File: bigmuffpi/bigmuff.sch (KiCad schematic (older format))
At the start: 63 parts, among them J1 PWR JACK, J4 OUTPUT, J5 INPUT, Q1 BC239, Q2 BC239, Q3 BC239, Q4 BC239

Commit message: add: assign footprint to PPTC
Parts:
- F1: footprint 1206 -> Capacitor_THT:C_Disc_D8.0mm_W2.5mm_P5.00mm
- gave numbers to parts that had none: 3
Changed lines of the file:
@@
 F 0 "F1" H 2650 5650 45  0000 C CNN
 F 1 "PPTC_HALF-AMP" H 2650 5550 45  0000 C CNN
-F 2 "1206" H 2600 5950 20  0001 C CNN
+F 2 "Capacitor_THT:C_Disc_D8.0mm_W2.5mm_P5.00mm" H 2600 5950 20  0001 C CNN
 F 3 "" H 2600 5750 50  0001 C CNN
 F 4 "RES-08585" H 2650 5450 60  0000 C CNN "Field4"
@@
 	1450 5350 3450 5350
 $Comp
-L Connector:TestPoint TP?
+L Connector:TestPoint TP7
 U 1 1 5F5852AE
 P 2450 3250
-F 0 "TP?" H 2300 3250 50  0000 R CNN
+F 0 "TP7" H 2300 3250 50  0000 R CNN
 F 1 "TestPoint" H 2400 3350 50  0000 R CNN
 F 2 "TestPoint:TestPoint_Pad_2.0x2.0mm" H 2650 3250 50  0001 C CNN
@@
 Connection ~ 2450 3300
 $Comp
-L Connector:TestPoint TP?
+L Connector:TestPoint TP8
 U 1 1 5F59ACBE
 P 4500 2500
-F 0 "TP?" H 4350 2500 50  0000 R CNN
+F 0 "TP8" H 4350 2500 50  0000 R CNN
 F 1 "TestPoint" H 4450 2600 50  0000 R CNN
 F 2 "TestPoint:TestPoint_Pad_2.0x2.0mm" H 4700 2500 50  0001 C CNN
@@
 Connection ~ 4500 2550
 $Comp
-L Connector:TestPoint TP?
+L Connector:TestPoint TP9
 U 1 1 5F5A9929
 P 6350 2500
-F 0 "TP?" H 6200 2500 50  0000 R CNN
+F 0 "TP9" H 6200 2500 50  0000 R CNN
 F 1 "TestPoint" H 6300 2600 50  0000 R CNN
 F 2 "TestPoint:TestPoint_Pad_2.0x2.0mm" H 6550 2500 50  0001 C CNN

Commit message: fix: minor name fix for PPTC
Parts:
- F1: value PPTC_HALF-AMP -> PPTC
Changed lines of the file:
@@
 P 2600 5750
 F 0 "F1" H 2650 5650 45  0000 C CNN
-F 1 "PPTC_HALF-AMP" H 2650 5550 45  0000 C CNN
+F 1 "PPTC" H 2650 5550 45  0000 C CNN
 F 2 "Capacitor_THT:C_Disc_D8.0mm_W2.5mm_P5.00mm" H 2600 5950 20  0001 C CNN
 F 3 "" H 2600 5750 50  0001 C CNN
-F 4 "RES-08585" H 2650 5450 60  0000 C CNN "Field4"
+F 4 "RES-08585" H 2650 5450 60  0001 C CNN "Field4"
 	1    2600 5750
 	1    0    0    -1

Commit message: add: pick PPTC component on mouser
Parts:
- F1: Mfr. No (none) -> MF-R020; Mouser (none) -> 652-MF-R020; Supplier (none) -> Mouser
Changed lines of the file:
@@
 F 1 "PPTC" H 2650 5550 45  0000 C CNN
 F 2 "Capacitor_THT:C_Disc_D8.0mm_W2.5mm_P5.00mm" H 2600 5950 20  0001 C CNN
-F 3 "" H 2600 5750 50  0001 C CNN
+F 3 "https://cz.mouser.com/datasheet/2/54/mfr-777680.pdf" H 2600 5750 50  0001 C CNN
 F 4 "RES-08585" H 2650 5450 60  0001 C CNN "Field4"
+F 5 "MF-R020" H 2600 5750 50  0001 C CNN "Mfr. No"
+F 6 "652-MF-R020 " H 2600 5750 50  0001 C CNN "Mouser"
+F 7 "Mouser" H 2600 5750 50  0001 C CNN "Supplier"
 	1    2600 5750
 	1    0    0    -1

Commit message: add: decoupling transistor
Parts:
- added C14: 1uF, Capacitor_THT:CP_Radial_D5.0mm_P2.00mm, symbol Device:CP1
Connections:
- net +9V: now also C14.1
- net GND: now also C14.2
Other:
- moved on the sheet: D6, F1, J1
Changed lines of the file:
@@
 L power:+9V #PWR019
 U 1 1 5EDC6BC5
-P 3100 5750
-F 0 "#PWR019" H 3100 5600 50  0001 C CNN
-F 1 "+9V" H 3115 5923 50  0000 C CNN
-F 2 "" H 3100 5750 50  0001 C CNN
-F 3 "" H 3100 5750 50  0001 C CNN
-	1    3100 5750
+P 3100 5650
+F 0 "#PWR019" H 3100 5500 50  0001 C CNN
+F 1 "+9V" H 3115 5823 50  0000 C CNN
+F 2 "" H 3100 5650 50  0001 C CNN
+F 3 "" H 3100 5650 50  0001 C CNN
+	1    3100 5650
 	1    0    0    -1
 $EndComp
@@
 Text Notes 3700 5300 0    129  ~ 0
 Foot Switch\n
-Text Notes 1550 5300 0    129  ~ 0
+Text Notes 1200 5300 0    129  ~ 0
 Power
 $Comp
@@
 L Connector:Barrel_Jack_Switch J1
 U 1 1 5F0D54E6
-P 1950 5750
-F 0 "J1" H 2007 6067 50  0000 C CNN
-F 1 "PWR JACK" H 2007 5976 50  0000 C CNN
-F 2 "Connector_PinHeader_2.54mm:PinHeader_1x03_P2.54mm_Vertical" H 2000 5710 50  0001 C CNN
-F 3 "https://www.aliexpress.com/wholesale?catId=0&SearchText=panel+mount+barrel+jack" H 2000 5710 50  0001 C CNN
-F 4 "" H 1950 5750 50  0001 C CNN "LCSC"
-F 5 "" H 1950 5750 50  0001 C CNN "Mfr. No"
-F 6 "Aliexpress" H 1950 5750 50  0001 C CNN "Supplier"
-	1    1950 5750
+P 1600 5750
+F 0 "J1" H 1657 6067 50  0000 C CNN
+F 1 "PWR JACK" H 1657 5976 50  0000 C CNN
+F 2 "Connector_PinHeader_2.54mm:PinHeader_1x03_P2.54mm_Vertical" H 1650 5710 50  0001 C CNN
+F 3 "https://www.aliexpress.com/wholesale?catId=0&SearchText=panel+mount+barrel+jack" H 1650 5710 50  0001 C CNN
+F 4 "" H 1600 5750 50  0001 C CNN "LCSC"
+F 5 "" H 1600 5750 50  0001 C CNN "Mfr. No"
+F 6 "Aliexpress" H 1600 5750 50  0001 C CNN "Supplier"
+	1    1600 5750
 	1    0    0    -1
 $EndComp
@@
 L Device:D D6
 U 1 1 5F0DF5EC
-P 3000 6000
-F 0 "D6" V 2950 6200 50  0000 C CNN
-F 1 "1N914" V 3050 6200 50  0000 C CNN
-F 2 "Diode_THT:D_DO-35_SOD27_P7.62mm_Horizontal" H 3000 6000 50  0001 C CNN
-F 3 "https://cz.mouser.com/datasheet/2/308/1N914-D-1801484.pdf" H 3000 6000 50  0001 C CNN
-F 4 "C125665" H 3000 6000 50  0001 C CNN "LCSC"
-F 5 "1N914" H 3000 6000 50  0001 C CNN "Mfr. No"
-F 6 "512-1N914" H 3000 6000 50  0001 C CNN "Mouser"
-F 7 "Mouser" H 3000 6000 50  0001 C CNN "Supplier"
-	1    3000 6000
+P 2650 6000
+F 0 "D6" V 2600 6200 50  0000 C CNN
+F 1 "1N914" V 2700 6200 50  0000 C CNN
+F 2 "Diode_THT:D_DO-35_SOD27_P7.62mm_Horizontal" H 2650 6000 50  0001 C CNN
+F 3 "https://cz.mouser.com/datasheet/2/308/1N914-D-1801484.pdf" H 2650 6000 50  0001 C CNN
+F 4 "C125665" H 2650 6000 50  0001 C CNN "LCSC"
+F 5 "1N914" H 2650 6000 50  0001 C CNN "Mfr. No"
+F 6 "512-1N914" H 2650 6000 50  0001 C CNN "Mouser"
+F 7 "Mouser" H 2650 6000 50  0001 C CNN "Supplier"
+	1    2650 6000
 	0    1    1    0
 $EndComp
@@
 L power:GND #PWR023
 U 1 1 5F12432A
-P 2400 5500
-F 0 "#PWR023" H 2400 5250 50  0001 C CNN
-F 1 "GND" H 2405 5327 50  0000 C CNN
-F 2 "" H 2400 5500 50  0001 C CNN
-F 3 "" H 2400 5500 50  0001 C CNN
-	1    2400 5500
+P 2050 5500
+F 0 "#PWR023" H 2050 5250 50  0001 C CNN
+F 1 "GND" H 2055 5327 50  0000 C CNN
+F 2 "" H 2050 5500 50  0001 C CNN
+F 3 "" H 2050 5500 50  0001 C CNN
+	1    2050 5500
 	1    0    0    -1
 $EndComp
@@
 	6200 5350 6200 7650
 Wire Wire Line
-	2250 5750 2300 5750
-Wire Wire Line
-	2250 5850 2300 5850
-Wire Wire Line
-	2300 5850 2300 5750
-Wire Wire Line
-	2250 5650 2250 5450
+	1900 5750 1950 5750
+Wire Wire Line
+	1900 5850 1950 5850
+Wire Wire Line
+	1950 5850 1950 5750
+Wire Wire Line
+	1900 5650 1900 5450
 $Comp
 L SparkFun-Fuses:PPTC_HALF-AMP F1
 U 1 1 5F449675
-P 2600 5750
-F 0 "F1" H 2650 5650 45  0000 C CNN
-F 1 "PPTC" H 2650 5550 45  0000 C CNN
-F 2 "Capacitor_THT:C_Disc_D8.0mm_W2.5mm_P5.00mm" H 2600 5950 20  0001 C CNN
-F 3 "https://cz.mouser.com/datasheet/2/54/mfr-777680.pdf" H 2600 5750 50  0001 C CNN
-F 4 "RES-08585" H 2650 5450 60  0001 C CNN "Field4"
-F 5 "MF-R020" H 2600 5750 50  0001 C CNN "Mfr. No"
-F 6 "652-MF-R020 " H 2600 5750 50  0001 C CNN "Mouser"
-F 7 "Mouser" H 2600 5750 50  0001 C CNN "Supplier"
-	1    2600 5750
+P 2250 5750
+F 0 "F1" H 2300 5650 45  0000 C CNN
+F 1 "PPTC" H 2300 5550 45  0000 C CNN
+F 2 "Capacitor_THT:C_Disc_D8.0mm_W2.5mm_P5.00mm" H 2250 5950 20  0001 C CNN
+F 3 "https://cz.mouser.com/datasheet/2/54/mfr-777680.pdf" H 2250 5750 50  0001 C CNN
+F 4 "RES-08585" H 2300 5450 60  0001 C CNN "Field4"
+F 5 "MF-R020" H 2250 5750 50  0001 C CNN "Mfr. No"
+F 6 "652-MF-R020 " H 2250 5750 50  0001 C CNN "Mouser"
+F 7 "Mouser" H 2250 5750 50  0001 C CNN "Supplier"
+	1    2250 5750
 	1    0    0    -1
 $EndComp
@@
 L power:GND #PWR020
 U 1 1 5F44D824
-P 3000 6250
-F 0 "#PWR020" H 3000 6000 50  0001 C CNN
-F 1 "GND" H 3005 6077 50  0000 C CNN
-F 2 "" H 3000 6250 50  0001 C CNN
-F 3 "" H 3000 6250 50  0001 C CNN
-	1    3000 6250
-	1    0    0    -1
-$EndComp
-Wire Wire Line
-	3000 6250 3000 6150
-Wire Wire Line
-	2900 5750 3000 5750
-Wire Wire Line
-	2400 5750 2300 5750
-Connection ~ 2300 5750
-Wire Wire Line
-	3000 5850 3000 5750
-Connection ~ 3000 5750
-Wire Wire Line
-	3000 5750 3100 5750
-Wire Wire Line
-	2250 5450 2400 5450
-Wire Wire Line
-	2400 5450 2400 5500
-Text Notes 1700 6400 0    50   ~ 0
+P 2650 6250
+F 0 "#PWR020" H 2650 6000 50  0001 C CNN
+F 1 "GND" H 2655 6077 50  0000 C CNN
+F 2 "" H 2650 6250 50  0001 C CNN
+F 3 "" H 2650 6250 50  0001 C CNN
+	1    2650 6250
+	1    0    0    -1
+$EndComp
+Wire Wire Line
+	2650 6250 2650 6150
+Wire Wire Line
+	2550 5750 2650 5750
+Wire Wire Line
+	2050 5750 1950 5750
+Connection ~ 1950 5750
+Wire Wire Line
+	2650 5850 2650 5750
+Connection ~ 2650 5750
+Wire Wire Line
+	1900 5450 2050 5450
+Wire Wire Line
+	2050 5450 2050 5500
+Text Notes 1350 6400 0    50   ~ 0
 Reverse Polarity Protection\nPPTC behaves like a fuse\nbut it's not one-time use
-Wire Notes Line
-	1450 5350 1450 6500
-Wire Notes Line
-	1450 6500 3450 6500
-Wire Notes Line
-	3450 6500 3450 5350
-Wire Notes Line
-	1450 5350 3450 5350
 $Comp
 L Connector:TestPoint TP7
@@
 	6350 2500 6350 2550
 Connection ~ 6350 2550
+$Comp
+L Device:CP1 C14
+U 1 1 5F60714F
+P 3100 6000
+F 0 "C14" H 3300 6050 50  0000 C CNN
+F 1 "1uF" H 3300 5950 50  0000 C CNN
+F 2 "Capacitor_THT:CP_Radial_D5.0mm_P2.00mm" H 3100 6000 50  0001 C CNN
+F 3 "https://cz.mouser.com/datasheet/2/445/860020672005-1725471.pdf" H 3100 6000 50  0001 C CNN
+F 4 "860020672005" H 3100 6000 50  0001 C CNN "Mfr. No"
+F 5 "710-860020672005" H 3100 6000 50  0001 C CNN "Mouser"
+F 6 "Mouser" H 3100 6000 50  0001 C CNN "Supplier"
+	1    3100 6000
+	1    0    0    -1
+$EndComp
+$Comp
+L power:GND #PWR024
+U 1 1 5F64BA01
+P 3100 6250
+F 0 "#PWR024" H 3100 6000 50  0001 C CNN
+F 1 "GND" H 3105 6077 50  0000 C CNN
+F 2 "" H 3100 6250 50  0001 C CNN
+F 3 "" H 3100 6250 50  0001 C CNN
+	1    3100 6250
+	1    0    0    -1
+$EndComp
+Wire Wire Line
+	3100 6250 3100 6150
+Wire Wire Line
+	3100 5750 3100 5850
+Wire Wire Line
+	2650 5750 3100 5750
+Wire Wire Line
+	3100 5650 3100 5750
+Connection ~ 3100 5750
+Wire Notes Line
+	3400 5350 3400 6550
+Wire Notes Line
+	3400 6550 1100 6550
+Wire Notes Line
+	1100 5350 1100 6550
+Wire Notes Line
+	1100 5350 3400 5350
 $EndSCHEMATC

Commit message: fix: transistor pin mapping
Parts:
- Q1, Q2, Q3, Q4: symbol Device:Q_NPN_BCE -> Device:Q_NPN_CBE
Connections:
- net at C1.1, C2.2, R2.1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: now also Q1.2 (B); no longer Q1.1 (B)
- net at C2.1, C3.2, R3.1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: now also Q1.1 (C); no longer Q1.2 (C)
- net at C5.2, C6.2, R7.2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: now also Q2.2 (B); no longer Q2.1 (B)
- net at C6.1, C7.2, D1.2 (A)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: now also Q2.1 (C); no longer Q2.2 (C)
- net at C8.2, C9.2, R12.2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: now also Q3.2 (B); no longer Q3.1 (B)
- net at C10.2, C9.1, D3.2 (A)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: now also Q3.1 (C); no longer Q3.2 (C)
- net at C12.1, R19.2, R20.1: now also Q4.2 (B); no longer Q4.1 (B)
- net at C13.2, R21.2: now also Q4.1 (C); no longer Q4.2 (C)
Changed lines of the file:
@@
 $EndComp
 $Comp
-L Device:Q_NPN_BCE Q1
+L Device:Q_NPN_CBE Q1
 U 1 1 5EB70D38
 P 2850 4000
@@
 $EndComp
 $Comp
-L Device:Q_NPN_BCE Q2
+L Device:Q_NPN_CBE Q2
 U 1 1 5EB996F1
 P 5150 3800
@@
 $EndComp
 $Comp
-L Device:Q_NPN_BCE Q4
+L Device:Q_NPN_CBE Q4
 U 1 1 5EC2E896
 P 9350 3550
@@
 $EndComp
 $Comp
-L Device:Q_NPN_BCE Q3
+L Device:Q_NPN_CBE Q3
 U 1 1 5EBD96C1
 P 7000 3800

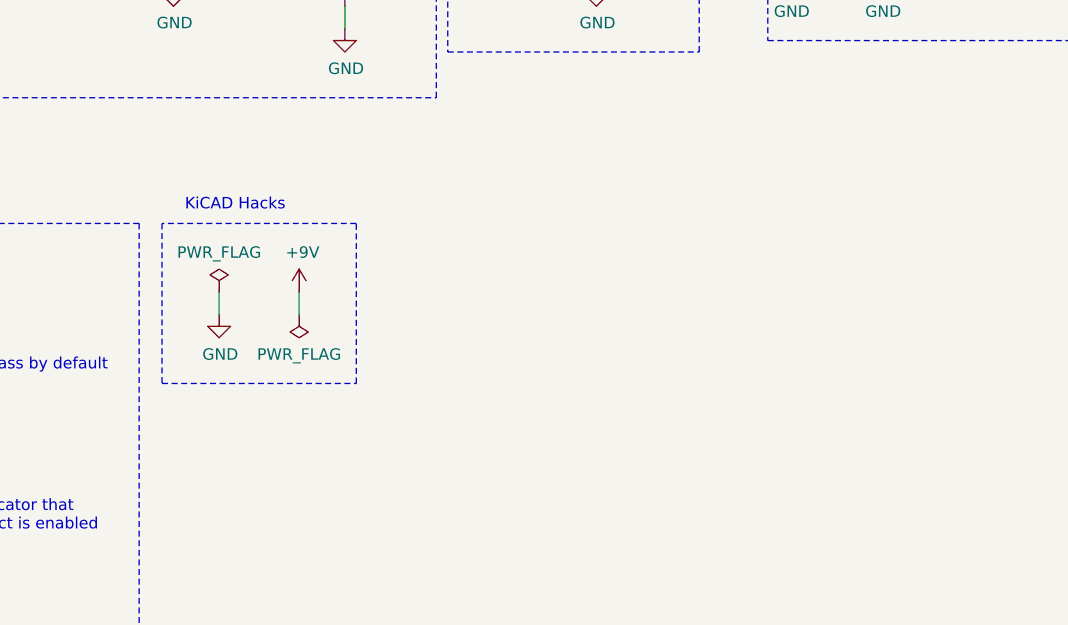
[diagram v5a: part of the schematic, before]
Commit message: add: wire connectors on schematics
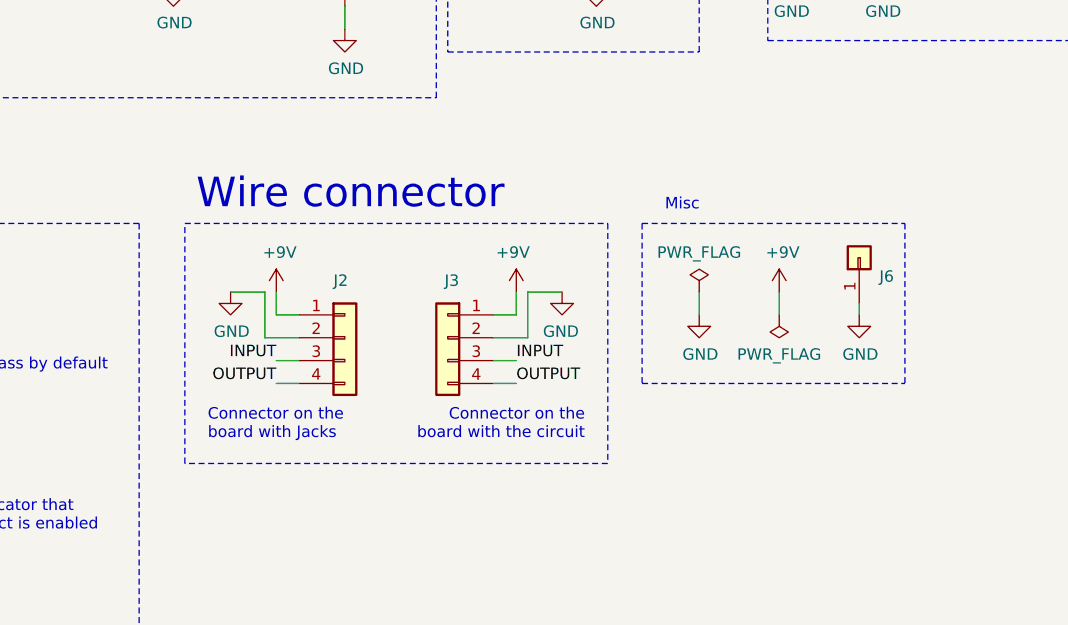
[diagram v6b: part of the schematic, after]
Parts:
- added J2: Wire connector (smol), Connector_PinHeader_2.54mm:PinHeader_1x03_P2.54mm_Vertical, symbol Connector_Generic:Conn_01x04
- added J3: Wire connector (circuit), Connector_PinHeader_2.54mm:PinHeader_1x03_P2.54mm_Vertical, symbol Connector_Generic:Conn_01x04
- added J6: GND for scope, Connector_PinHeader_2.54mm:PinHeader_1x01_P2.54mm_Vertical, symbol Connector_Generic:Conn_01x01
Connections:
- net +9V: now also J2.1 (Pin_1), J3.1 (Pin_1)
- net GND: now also J2.2 (Pin_2), J3.2 (Pin_2), J6.1 (Pin_1)
- net INPUT: now also J2.3 (Pin_3), J3.3 (Pin_3)
- net OUTPUT: now also J2.4 (Pin_4), J3.4 (Pin_4)
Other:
- note added: "Connector on the \nboard with Jacks"
- note added: "Connector on the \nboard with the circuit\n"
- note added: "Misc"
- note added: "Wire connector"
- note removed: "KiCAD Hacks"
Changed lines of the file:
@@
 L power:PWR_FLAG #FLG0101
 U 1 1 5F01DC13
-P 6550 5650
-F 0 "#FLG0101" H 6550 5725 50  0001 C CNN
-F 1 "PWR_FLAG" H 6550 5823 50  0000 C CNN
-F 2 "" H 6550 5650 50  0001 C CNN
-F 3 "~" H 6550 5650 50  0001 C CNN
-	1    6550 5650
+P 8650 5650
+F 0 "#FLG0101" H 8650 5725 50  0001 C CNN
+F 1 "PWR_FLAG" H 8650 5823 50  0000 C CNN
+F 2 "" H 8650 5650 50  0001 C CNN
+F 3 "~" H 8650 5650 50  0001 C CNN
+	1    8650 5650
 	1    0    0    -1
 $EndComp
@@
 L power:PWR_FLAG #FLG0102
 U 1 1 5F0203A8
-P 6900 5750
-F 0 "#FLG0102" H 6900 5825 50  0001 C CNN
-F 1 "PWR_FLAG" H 6900 5923 50  0000 C CNN
-F 2 "" H 6900 5750 50  0001 C CNN
-F 3 "~" H 6900 5750 50  0001 C CNN
-	1    6900 5750
+P 9000 5750
+F 0 "#FLG0102" H 9000 5825 50  0001 C CNN
+F 1 "PWR_FLAG" H 9000 5923 50  0000 C CNN
+F 2 "" H 9000 5750 50  0001 C CNN
+F 3 "~" H 9000 5750 50  0001 C CNN
+	1    9000 5750
 	-1   0    0    1
 $EndComp
@@
 L power:+9V #PWR0101
 U 1 1 5F024120
-P 6900 5650
-F 0 "#PWR0101" H 6900 5500 50  0001 C CNN
-F 1 "+9V" H 6915 5823 50  0000 C CNN
-F 2 "" H 6900 5650 50  0001 C CNN
-F 3 "" H 6900 5650 50  0001 C CNN
-	1    6900 5650
+P 9000 5650
+F 0 "#PWR0101" H 9000 5500 50  0001 C CNN
+F 1 "+9V" H 9015 5823 50  0000 C CNN
+F 2 "" H 9000 5650 50  0001 C CNN
+F 3 "" H 9000 5650 50  0001 C CNN
+	1    9000 5650
 	1    0    0    -1
 $EndComp
@@
 L power:GND #PWR0102
 U 1 1 5F024502
-P 6550 5750
-F 0 "#PWR0102" H 6550 5500 50  0001 C CNN
-F 1 "GND" H 6555 5577 50  0000 C CNN
-F 2 "" H 6550 5750 50  0001 C CNN
-F 3 "" H 6550 5750 50  0001 C CNN
-	1    6550 5750
-	1    0    0    -1
-$EndComp
-Wire Wire Line
-	6550 5750 6550 5650
-Wire Wire Line
-	6900 5750 6900 5650
-Wire Notes Line
-	6300 5350 6300 6050
-Wire Notes Line
-	6300 6050 7150 6050
-Wire Notes Line
-	7150 6050 7150 5350
-Wire Notes Line
-	7150 5350 6300 5350
-Text Notes 6400 5300 0    50   ~ 0
-KiCAD Hacks
+P 8650 5750
+F 0 "#PWR0102" H 8650 5500 50  0001 C CNN
+F 1 "GND" H 8655 5577 50  0000 C CNN
+F 2 "" H 8650 5750 50  0001 C CNN
+F 3 "" H 8650 5750 50  0001 C CNN
+	1    8650 5750
+	1    0    0    -1
+$EndComp
+Wire Wire Line
+	8650 5750 8650 5650
+Wire Wire Line
+	9000 5750 9000 5650
+Wire Notes Line
+	8400 5350 8400 6050
+Text Notes 8500 5300 0    50   ~ 0
+Misc
 Wire Notes Line
 	3550 5350 3550 7650
@@
 Wire Notes Line
 	1100 5350 3400 5350
+$Comp
+L Connector_Generic:Conn_01x04 J3
+U 1 1 5F45FE6C
+P 7550 5850
+F 0 "J3" H 7500 6100 50  0000 L CNN
+F 1 "Wire connector (circuit)" H 7500 6100 50  0001 L CNN
+F 2 "Connector_PinHeader_2.54mm:PinHeader_1x03_P2.54mm_Vertical" H 7550 5850 50  0001 C CNN
+F 3 "~" H 7550 5850 50  0001 C CNN
+	1    7550 5850
+	-1   0    0    -1
+$EndComp
+Text Label 7850 5950 0    50   ~ 0
+INPUT
+Text Label 7850 6050 0    50   ~ 0
+OUTPUT
+Wire Wire Line
+	7850 5950 7750 5950
+Wire Wire Line
+	7850 6050 7750 6050
+$Comp
+L power:+9V #PWR027
+U 1 1 5F48AB78
+P 7850 5650
+F 0 "#PWR027" H 7850 5500 50  0001 C CNN
+F 1 "+9V" H 7865 5823 50  0000 C CNN
+F 2 "" H 7850 5650 50  0001 C CNN
+F 3 "" H 7850 5650 50  0001 C CNN
+	1    7850 5650
+	-1   0    0    -1
+$EndComp
+Wire Wire Line
+	7850 5650 7850 5750
+Wire Wire Line
+	7850 5750 7750 5750
+$Comp
+L power:GND #PWR028
+U 1 1 5F492500
+P 8050 5650
+F 0 "#PWR028" H 8050 5400 50  0001 C CNN
+F 1 "GND" H 8055 5477 50  0000 C CNN
+F 2 "" H 8050 5650 50  0001 C CNN
+F 3 "" H 8050 5650 50  0001 C CNN
+	1    8050 5650
+	-1   0    0    -1
+$EndComp
+Wire Wire Line
+	8050 5650 7900 5650
+Wire Wire Line
+	7900 5650 7900 5850
+Wire Wire Line
+	7900 5850 7750 5850
+Text Notes 8150 6300 2    50   ~ 0
+Connector on the \nboard with the circuit\n
+$Comp
+L Connector_Generic:Conn_01x04 J2
+U 1 1 5F4B5E99
+P 7100 5850
+F 0 "J2" H 7050 6100 50  0000 L CNN
+F 1 "Wire connector (smol)" H 7050 6100 50  0001 L CNN
+F 2 "Connector_PinHeader_2.54mm:PinHeader_1x03_P2.54mm_Vertical" H 7100 5850 50  0001 C CNN
+F 3 "~" H 7100 5850 50  0001 C CNN
+	1    7100 5850
+	1    0    0    -1
+$EndComp
+Text Label 6800 5950 2    50   ~ 0
+INPUT
+Text Label 6800 6050 2    50   ~ 0
+OUTPUT
+Wire Wire Line
+	6800 5950 6900 5950
+Wire Wire Line
+	6800 6050 6900 6050
+$Comp
+L power:+9V #PWR026
+U 1 1 5F4B5EA3
+P 6800 5650
+F 0 "#PWR026" H 6800 5500 50  0001 C CNN
+F 1 "+9V" H 6815 5823 50  0000 C CNN
+F 2 "" H 6800 5650 50  0001 C CNN
+F 3 "" H 6800 5650 50  0001 C CNN
+	1    6800 5650
+	1    0    0    -1
+$EndComp
+Wire Wire Line
+	6800 5650 6800 5750
+Wire Wire Line
+	6800 5750 6900 5750
+$Comp
+L power:GND #PWR025
+U 1 1 5F4B5EAB
+P 6600 5650
+F 0 "#PWR025" H 6600 5400 50  0001 C CNN
+F 1 "GND" H 6605 5477 50  0000 C CNN
+F 2 "" H 6600 5650 50  0001 C CNN
+F 3 "" H 6600 5650 50  0001 C CNN
+	1    6600 5650
+	1    0    0    -1
+$EndComp
+Wire Wire Line
+	6600 5650 6750 5650
+Wire Wire Line
+	6750 5650 6750 5850
+Wire Wire Line
+	6750 5850 6900 5850
+Text Notes 6500 6300 0    50   ~ 0
+Connector on the \nboard with Jacks
+Wire Notes Line
+	8250 5350 8250 6400
+Wire Notes Line
+	8250 6400 6400 6400
+Wire Notes Line
+	6400 6400 6400 5350
+Wire Notes Line
+	6400 5350 8250 5350
+Text Notes 6450 5300 0    129  ~ 0
+Wire connector
+$Comp
+L Connector_Generic:Conn_01x01 J6
+U 1 1 5F5C22D3
+P 9350 5500
+F 0 "J6" V 9268 5412 50  0000 R CNN
+F 1 "GND for scope" V 9223 5412 50  0001 R CNN
+F 2 "Connector_PinHeader_2.54mm:PinHeader_1x01_P2.54mm_Vertical" H 9350 5500 50  0001 C CNN
+F 3 "~" H 9350 5500 50  0001 C CNN
+	1    9350 5500
+	0    -1   -1   0
+$EndComp
+$Comp
+L power:GND #PWR029
+U 1 1 5F5C3191
+P 9350 5750
+F 0 "#PWR029" H 9350 5500 50  0001 C CNN
+F 1 "GND" H 9355 5577 50  0000 C CNN
+F 2 "" H 9350 5750 50  0001 C CNN
+F 3 "" H 9350 5750 50  0001 C CNN
+	1    9350 5750
+	1    0    0    -1
+$EndComp
+Wire Wire Line
+	9350 5750 9350 5700
+Wire Notes Line
+	9550 5350 9550 6050
+Wire Notes Line
+	8400 5350 9550 5350
+Wire Notes Line
+	8400 6050 9550 6050
 $EndSCHEMATC

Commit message: fix: wrong footprint for connectors
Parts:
- J2, J3: footprint Connector_PinHeader_2.54mm:PinHeader_1x03_P2.54mm_Vertical -> Connector_PinHeader_2.54mm:PinHeader_1x04_P2.54mm_Vertical
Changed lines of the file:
@@
 F 0 "J3" H 7500 6100 50  0000 L CNN
 F 1 "Wire connector (circuit)" H 7500 6100 50  0001 L CNN
-F 2 "Connector_PinHeader_2.54mm:PinHeader_1x03_P2.54mm_Vertical" H 7550 5850 50  0001 C CNN
+F 2 "Connector_PinHeader_2.54mm:PinHeader_1x04_P2.54mm_Vertical" H 7550 5850 50  0001 C CNN
 F 3 "~" H 7550 5850 50  0001 C CNN
 	1    7550 5850
@@
 F 0 "J2" H 7050 6100 50  0000 L CNN
 F 1 "Wire connector (smol)" H 7050 6100 50  0001 L CNN
-F 2 "Connector_PinHeader_2.54mm:PinHeader_1x03_P2.54mm_Vertical" H 7100 5850 50  0001 C CNN
+F 2 "Connector_PinHeader_2.54mm:PinHeader_1x04_P2.54mm_Vertical" H 7100 5850 50  0001 C CNN
 F 3 "~" H 7100 5850 50  0001 C CNN
 	1    7100 5850

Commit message: refactor: changed notes
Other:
- note added: "Board with Jacks"
- note added: "Board with the circuit\n"
- note added: "Reverse Polarity Protection\nPPTC behaves like a fuse\nbut it's resetable"
- note removed: "Connector on the \nboard with Jacks"
- note removed: "Connector on the \nboard with the circuit\n"
- note removed: "Reverse Polarity Protection\nPPTC behaves like a fuse\nbut it's not one-time use"
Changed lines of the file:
@@
 	2050 5450 2050 5500
 Text Notes 1350 6400 0    50   ~ 0
-Reverse Polarity Protection\nPPTC behaves like a fuse\nbut it's not one-time use
+Reverse Polarity Protection\nPPTC behaves like a fuse\nbut it's resetable
 $Comp
 L Connector:TestPoint TP7
@@
 Wire Wire Line
 	7900 5850 7750 5850
-Text Notes 8150 6300 2    50   ~ 0
-Connector on the \nboard with the circuit\n
+Text Notes 8150 6250 2    50   ~ 0
+Board with the circuit\n
 $Comp
 L Connector_Generic:Conn_01x04 J2
@@
 Wire Wire Line
 	6750 5850 6900 5850
-Text Notes 6500 6300 0    50   ~ 0
-Connector on the \nboard with Jacks
+Text Notes 6500 6250 0    50   ~ 0
+Board with Jacks
 Wire Notes Line
 	8250 5350 8250 6400
